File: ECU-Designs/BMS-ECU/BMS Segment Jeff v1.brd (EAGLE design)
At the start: 110 x 130.8 mm, 95 parts, among them T1 NPN_BCP56T1, X1 MINIFIT_5566-2, X2 To Positive BMS

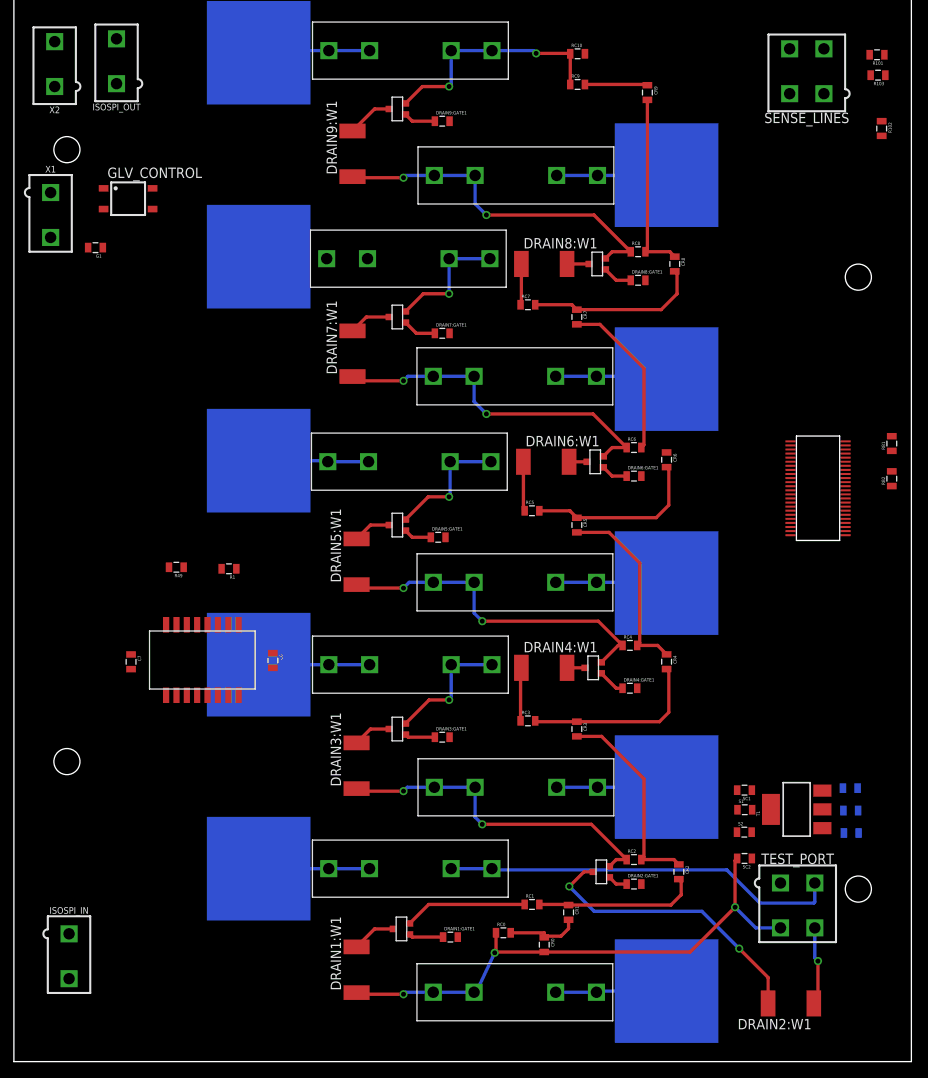
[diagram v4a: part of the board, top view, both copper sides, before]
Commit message: More BMS trace updates
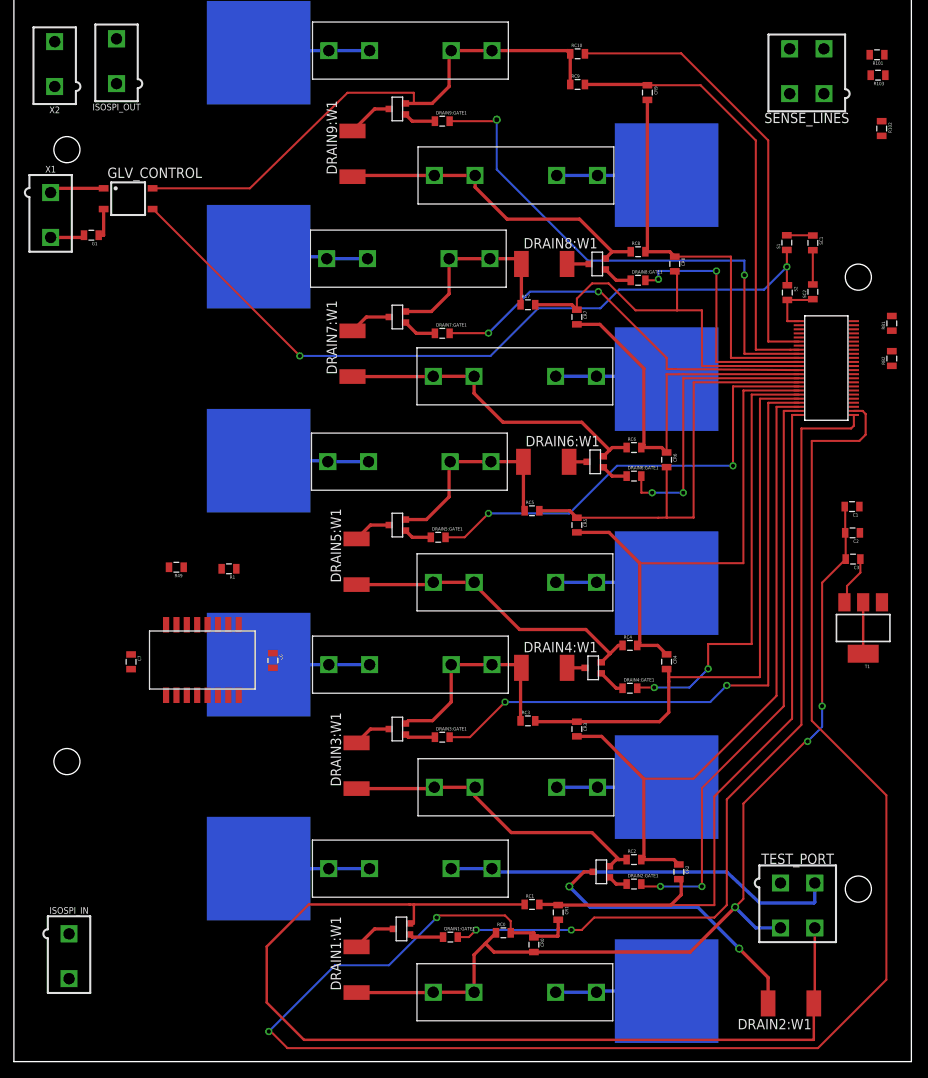
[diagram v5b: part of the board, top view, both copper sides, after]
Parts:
- moved SC2 70.0 mm to (97.9, 117.6), turned to 90 degrees
- moved S1 69.7 mm to (94.7, 123.6), turned to 90 degrees
- moved SC1 67.6 mm to (97.9, 123.6), turned to 270 degrees
- moved S2 66.3 mm to (94.8, 117.5), turned to 270 degrees
- moved C1 40.0 mm to (102.7, 91.3), flipped to the top
- moved C2 34.0 mm to (102.8, 88.0), flipped to the top
- moved C3 28.1 mm to (102.8, 84.8), flipped to the top
- moved T1 23.7 mm to (104.1, 76.4), turned to 180 degrees
- moved U$2 14.8 mm to (99.6, 108.2)
- moved RB1 14.7 mm to (107.6, 113.7)
- moved RB2 14.7 mm to (107.6, 109.4)
- moved G1 1.61 mm to (9.49, 124.5)
- moved CR0 1.27 mm to (63.7, 37.6)
- moved CR1 1.27 mm to (66.7, 41.5)
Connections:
- net N$10 renamed SSR-
- net N$11 renamed SSR+
- net N$3 renamed SUPPLY_INTER
- net CC9: no longer X2.1, X2.2
- net SENSE9: now also X2.1, X2.2
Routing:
- net C0: track 9.18 -> 206.8 mm, vias 0 -> 2
- net S1: track 0.00 -> 104.7 mm, vias 0 -> 2
- net SENSE1_J: track 24.7 -> 126.3 mm, vias 1 -> 0
- net SUPPLY_INTER: track 0.00 -> 94.1 mm, vias 0 -> 2
- net S3: track 0.00 -> 80.1 mm, vias 0 -> 2
- net S2: track 0.00 -> 72.0 mm, vias 0 -> 2
- net C1: track 20.0 -> 90.1 mm
- net S9: track 0.00 -> 65.1 mm, vias 0 -> 2
- net C2: track 25.3 -> 83.9 mm
- net S5: track 0.00 -> 56.7 mm, vias 0 -> 2
- net C10: track 0.00 -> 55.3 mm
- net V-: track 67.2 -> 121.9 mm
- net S4: track 0.00 -> 54.5 mm, vias 0 -> 2
- net C3: track 22.3 -> 72.9 mm
- net S7: track 0.00 -> 49.6 mm, vias 0 -> 2
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
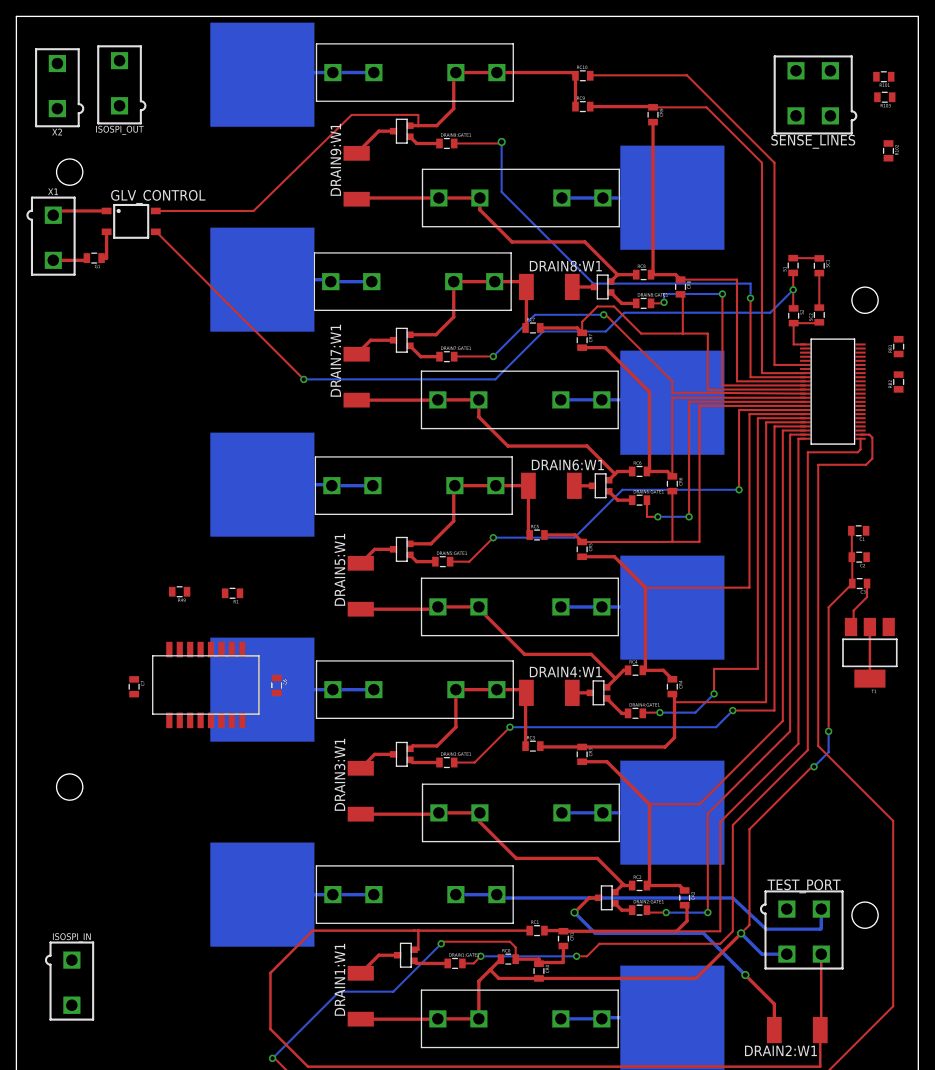
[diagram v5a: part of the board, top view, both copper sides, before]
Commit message: Finished Negative Side BMS Board Layout
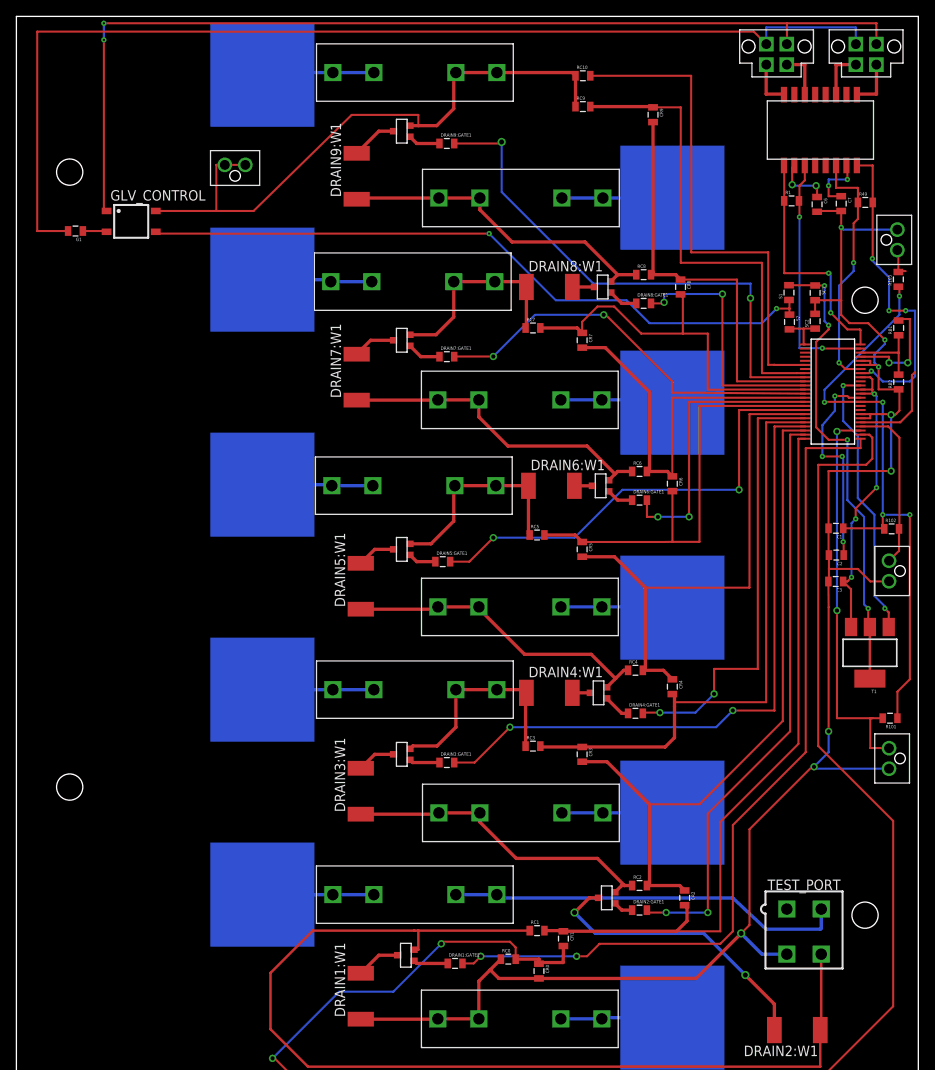
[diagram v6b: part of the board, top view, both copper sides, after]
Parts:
- removed ISOSPI_IN, ISOSPI_OUT, X1: MINIFIT_5566-2, HyTechDevices:MINIFIT_5566-2
- removed SENSE_LINES: MINIFIT_5566-4, HyTechDevices:MINIFIT_5566-4
- removed X2: To Positive BMS, HyTechDevices:MINIFIT_5566-2
- added BMSIN, BMSOUT: CONNECTOR-4NANO-FIT-VERTICAL-4, HyTechDevices:NANO-FIT_VERTICAL-4
- added TO_TOP: CONNECTOR-2NANO-FIT_VERTICAL-2, HyTechDevices:NANO-FIT_VERTICAL-2
- added X3: Th1, HyTechDevices:NANO-FIT_VERTICAL-2
- added X4: Th2, HyTechDevices:NANO-FIT_VERTICAL-2
- added X5: Th3, HyTechDevices:NANO-FIT_VERTICAL-2
- moved C7 104.4 mm to (100.6, 131.2)
- moved TRANSFORMER- 101.0 mm to (98.1, 140.1), turned to 90 degrees
- moved R49 96.2 mm to (103.5, 131.3), turned to 0 degrees
- moved C6 88.2 mm to (97.7, 131.1)
- moved R1 83.3 mm to (94.5, 131.5), turned to 0 degrees
- moved R101 78.2 mm to (106.6, 68.4)
- moved R102 46.1 mm to (106.7, 91.5), turned to 0 degrees
- moved R103 22.3 mm to (107.6, 121.9), turned to 90 degrees
- moved G1 4.02 mm to (7.21, 127.8)
- moved S1 3.34 mm to (94.2, 120.3)
- moved SC1 3.34 mm to (97.4, 120.3)
- moved C3 2.93 mm to (99.9, 85.1)
- moved C2 2.81 mm to (100.0, 88.3)
- moved C1 2.80 mm to (99.9, 91.6)
- moved RB1 2.29 mm to (107.6, 116.0)
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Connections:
- removed net CURRENT_SENSE: SENSE_LINES.4, U$2.32
- removed net SSR+: GLV_CONTROL.1, X1.1
- new net SHUTDOWN_CIRCUIT: BMSIN.P$1, BMSOUT.P$1, GLV_CONTROL.1
- net GND: now also BMSIN.P$2, BMSOUT.P$2; no longer X1.2
- net ISOSPI-M_IN: now also BMSIN.P$3; no longer ISOSPI_IN.2
- net ISOSPI-M_OUT: now also BMSOUT.P$3; no longer ISOSPI_OUT.2
- net ISOSPI-P_IN: now also BMSIN.P$4; no longer ISOSPI_IN.1
- net ISOSPI-P_OUT: now also BMSOUT.P$4; no longer ISOSPI_OUT.1
- net SENSE9: now also TO_TOP.P$1, TO_TOP.P$2; no longer X2.1, X2.2
- net THERMISTOR1: now also R101.2, X5.P$2; no longer R103.2, SENSE_LINES.1
- net THERMISTOR2: now also X4.P$2; no longer SENSE_LINES.2
- net THERMISTOR3: now also R103.2, X3.P$2; no longer R101.2, SENSE_LINES.3
- net V-: now also X3.P$1, X4.P$1, X5.P$1
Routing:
- net GND: track 4.37 -> 132.6 mm
- net SHUTDOWN_CIRCUIT: track 0.00 -> 122.4 mm, vias 0 -> 2
- net V-: track 121.9 -> 212.5 mm, vias 3 -> 8
- net VREF2: track 0.00 -> 74.5 mm, vias 0 -> 5
- net THERMISTOR1: track 0.00 -> 49.7 mm, vias 0 -> 2
- net SUPPLY: track 9.50 -> 57.2 mm, vias 0 -> 4
- net N$9: track 0.00 -> 39.2 mm, vias 0 -> 4
- net DRIVE: track 0.00 -> 33.9 mm, vias 0 -> 2
- net VREG: track 6.11 -> 38.1 mm, vias 0 -> 4
- net N$8: track 0.00 -> 30.7 mm, vias 0 -> 2
- net N$42: track 0.00 -> 30.1 mm, vias 0 -> 2
- net N$5: track 0.00 -> 29.9 mm, vias 0 -> 2
- net VREF1: track 0.00 -> 25.7 mm, vias 0 -> 4
- net THERMISTOR2: track 0.00 -> 20.8 mm
- net THERMISTOR3: track 0.00 -> 15.4 mm
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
